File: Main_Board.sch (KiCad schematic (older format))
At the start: 62 parts, among them J1 DAC_12-bits, J2 Measurement_Header, Q1 Q_PNP_BCE, Q2 Q_NPN_BCE, U1 AD667, U2 LF356, U3 AD558JN

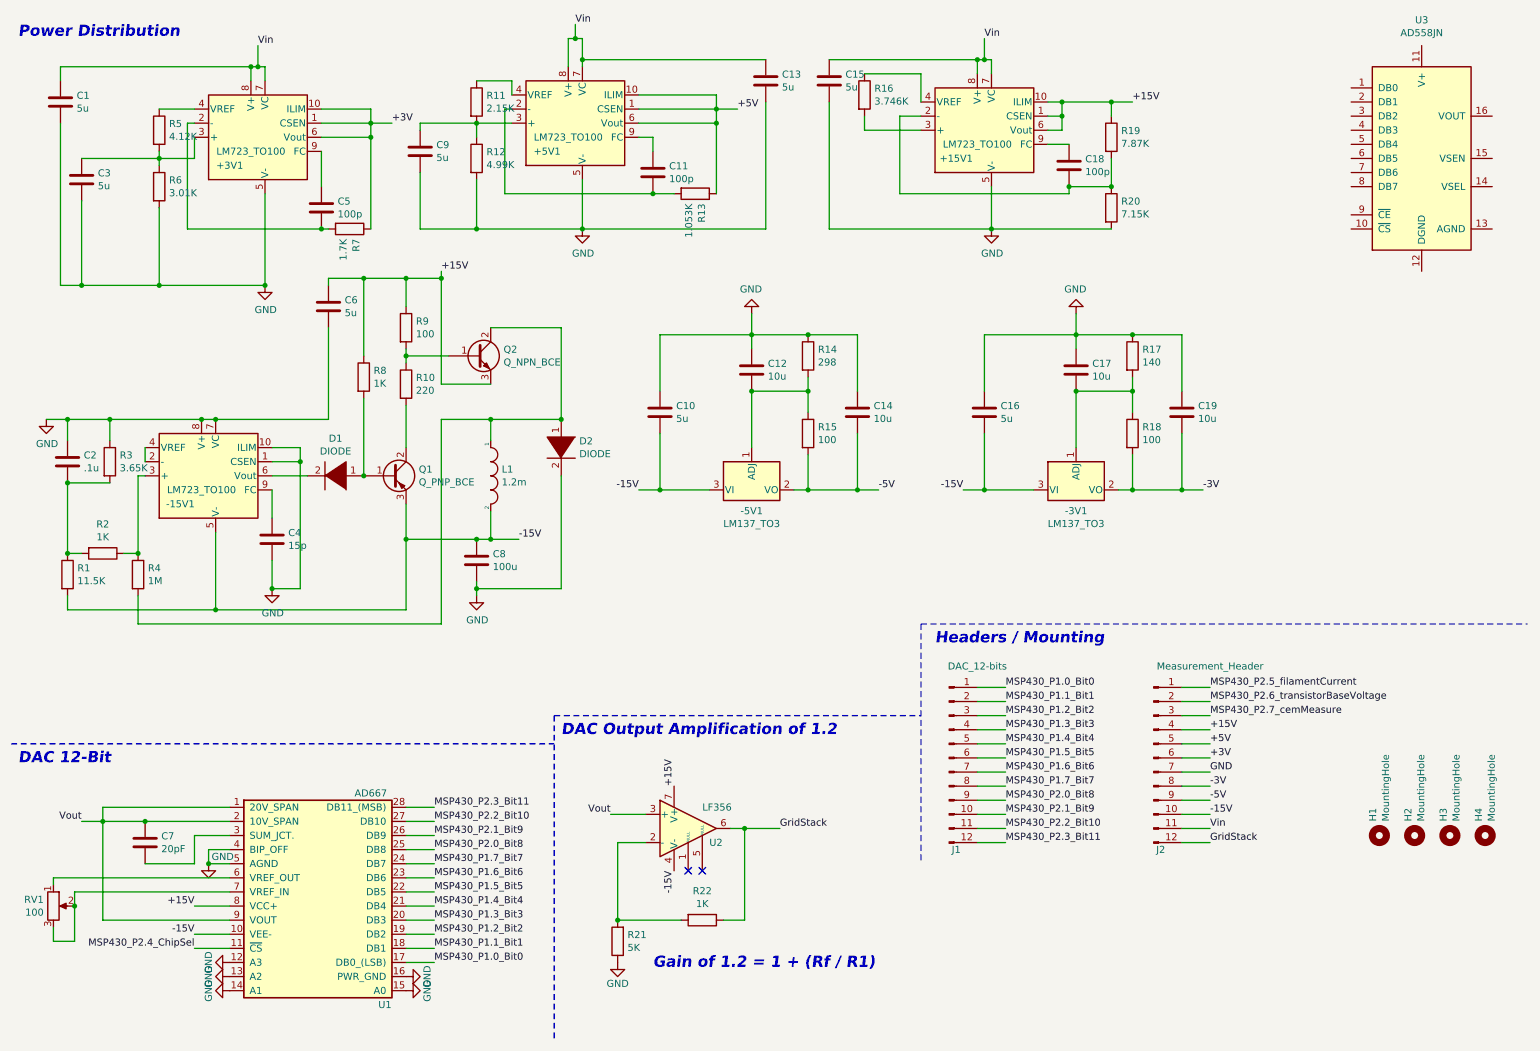
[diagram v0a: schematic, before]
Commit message: Defined and added 8-bit DAC for CEM transistor base voltage control to schematic and  layout. Still need to do the routing, waiting on clarification of analog output voltage range of 0-2.56V or 0-10V from Riya as this will effect 8-bit DAC pin wiring.
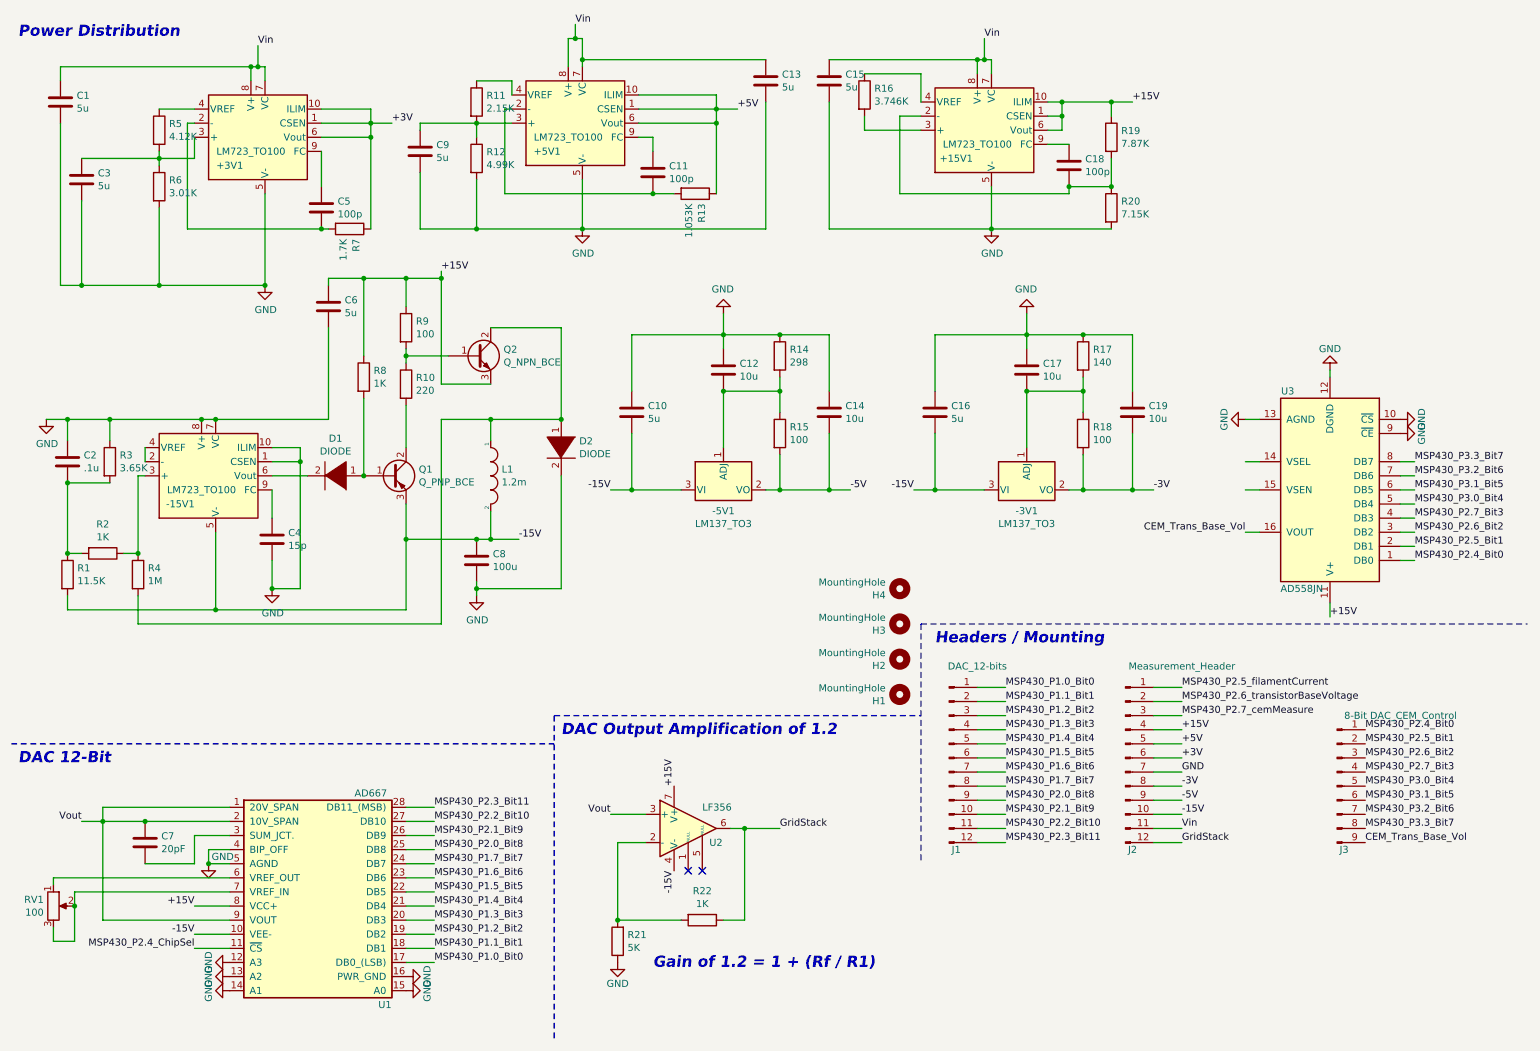
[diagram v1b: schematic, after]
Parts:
- added J3: 8-Bit DAC_CEM_Control, Connector_PinHeader_2.54mm:PinHeader_1x09_P2.54mm_Vertical, symbol Connector:Conn_01x09_Male
- RV1: footprint Potentiometer_THT:Potentiometer_Vishay_148-149_Single_Horizontal -> Potentiometer_THT:Potentiometer_Bourns_3299W_Vertical
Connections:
- net +15V: now also U3.11 (V+)
- net GND: now also U3.10 (~CS), U3.12 (DGND), U3.13 (AGND), U3.9 (~CE)
- net MSP430_P2.4_Bit0: now reaches U3.1 (DB0)
- net MSP430_P2.4_Bit0: now also J3.1 (Pin_1)
- net CEM_Trans_Base_Vol: now reaches U3.16 (VOUT)
- net CEM_Trans_Base_Vol: now also J3.9 (Pin_9)
- net MSP430_P2.5_Bit1: now reaches U3.2 (DB1)
- net MSP430_P2.5_Bit1: now also J3.2 (Pin_2)
- net MSP430_P2.6_Bit2: now reaches U3.3 (DB2)
- net MSP430_P2.6_Bit2: now also J3.3 (Pin_3)
- net MSP430_P2.7_Bit3: now reaches U3.4 (DB3)
- net MSP430_P2.7_Bit3: now also J3.4 (Pin_4)
- net MSP430_P3.0_Bit4: now reaches U3.5 (DB4)
- net MSP430_P3.0_Bit4: now also J3.5 (Pin_5)
- net MSP430_P3.1_Bit5: now reaches U3.6 (DB5)
- net MSP430_P3.1_Bit5: now also J3.6 (Pin_6)
- net MSP430_P3.2_Bit6: now reaches U3.7 (DB6)
- net MSP430_P3.2_Bit6: now also J3.7 (Pin_7)
- net MSP430_P3.3_Bit7: now reaches U3.8 (DB7)
- net MSP430_P3.3_Bit7: now also J3.8 (Pin_8)
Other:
- moved on the sheet: -3V1, -5V1, C10, C12, C14, C16, C17, C19, H1, H2, H3, H4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

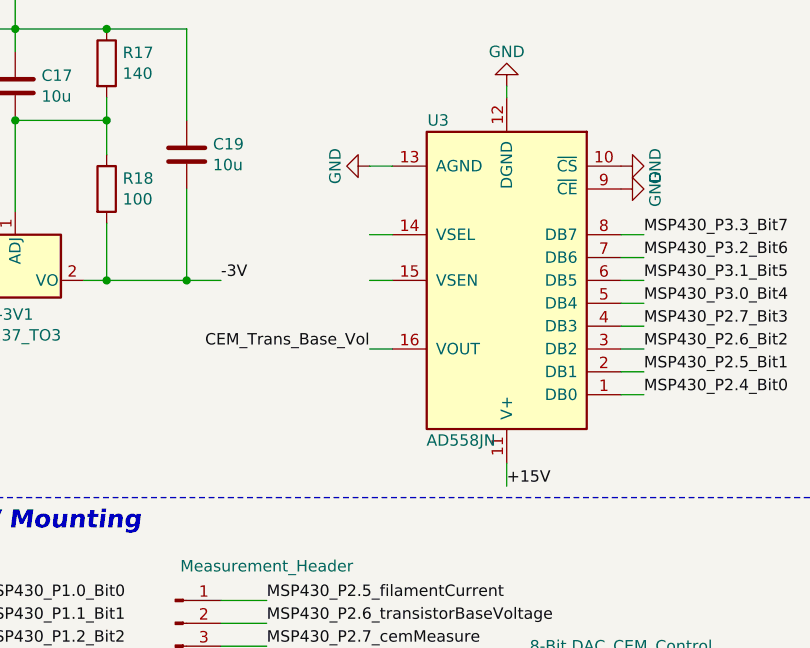
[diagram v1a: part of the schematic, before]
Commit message: Finished schematic and layout of 8-bit DAC for CEM transistor control. Adding GND plane to bottom copper.
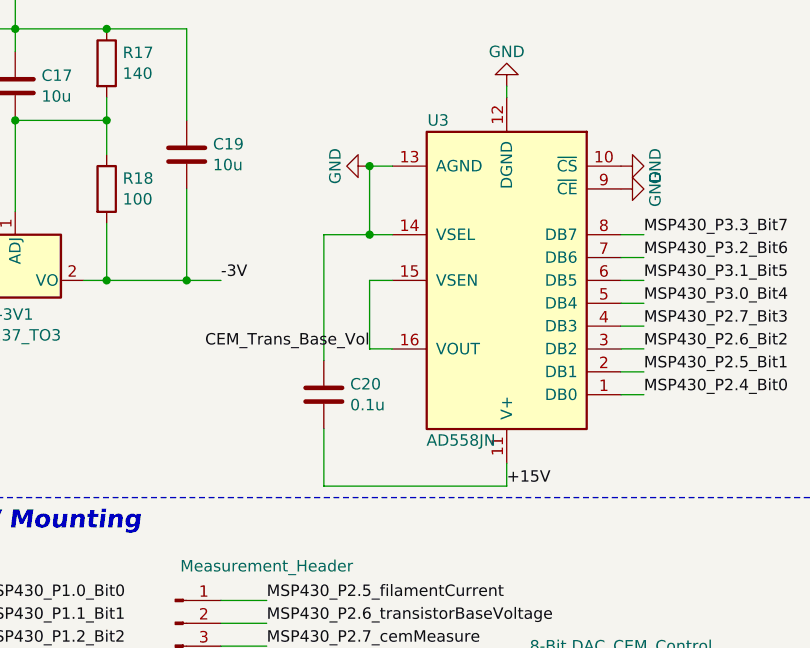
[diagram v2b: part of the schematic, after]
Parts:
- added C20: 0.1u, Capacitor_SMD:C_0805_2012Metric, symbol Device:C
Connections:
- net +15V: now also C20.2
- net CEM_Trans_Base_Vol: now also U3.15 (VSEN)
- net GND: now also U3.14 (VSEL), C20.1
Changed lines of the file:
@@
 Text Label 10100 6400 0    50   ~ 0
 CEM_Trans_Base_Vol
+Wire Wire Line
+	9250 3900 9250 4200
+Wire Wire Line
+	9250 3700 9250 3400
+Connection ~ 9250 3400
+Wire Wire Line
+	9250 3700 9050 3700
+Wire Wire Line
+	9050 4800 9850 4800
+Connection ~ 9250 3700
+$Comp
+L Device:C C20
+U 1 1 5E5EB6F5
+P 9050 4400
+F 0 "C20" H 9165 4446 50  0000 L CNN
+F 1 "0.1u" H 9165 4355 50  0000 L CNN
+F 2 "Capacitor_SMD:C_0805_2012Metric" H 9088 4250 50  0001 C CNN
+F 3 "~" H 9050 4400 50  0001 C CNN
+	1    9050 4400
+	1    0    0    -1
+$EndComp
+Wire Wire Line
+	9050 3700 9050 4250
+Wire Wire Line
+	9050 4800 9050 4550
 $EndSCHEMATC

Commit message: Update Schematic
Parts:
- removed J3: 8-Bit DAC_CEM_Control, Connector_PinHeader_2.54mm:PinHeader_1x09_P2.54mm_Vertical, symbol Connector:Conn_01x09_Male
- added J3: Measurement_Header, Connector_PinHeader_2.54mm:PinHeader_1x12_P2.54mm_Vertical, symbol Connector:Conn_01x12_Male
- J2: value Measurement_Header -> Bias_Header
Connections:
- net CEM_Trans_Base_Vol is gone; now on net MSP430_P2.6_transistorBaseVoltage: U3.15 (VSEN), U3.16 (VOUT)
- net +15V: now also J2.10 (Pin_10); no longer J2.4 (Pin_4)
- net +3V: now also J2.8 (Pin_8); no longer J2.6 (Pin_6)
- net +5V: now also J2.9 (Pin_9); no longer J2.5 (Pin_5)
- net -15V: now also J2.4 (Pin_4); no longer J2.10 (Pin_10)
- net -3V: now also J2.6 (Pin_6); no longer J2.8 (Pin_8)
- net -5V: now also J2.5 (Pin_5); no longer J2.9 (Pin_9)
- net MSP430_P2.4_Bit0: now also J3.1 (Pin_1)
- net MSP430_P2.5_Bit1: now also J3.2 (Pin_2)
- net MSP430_P2.5_filamentCurrent: now also J3.10 (Pin_10); no longer J2.1 (Pin_1)
- net MSP430_P2.6_Bit2: now also J3.3 (Pin_3)
- net MSP430_P2.6_transistorBaseVoltage: now also J3.12 (Pin_12); no longer J2.2 (Pin_2)
- net MSP430_P2.7_Bit3: now also J3.4 (Pin_4)
- net MSP430_P2.7_cemMeasure: now also J3.11 (Pin_11); no longer J2.3 (Pin_3)
- net MSP430_P3.0_Bit4: now also J3.5 (Pin_5)
- net MSP430_P3.1_Bit5: now also J3.6 (Pin_6)
- net MSP430_P3.2_Bit6: now also J3.7 (Pin_7)
- net MSP430_P3.3_Bit7: now also J3.8 (Pin_8)
- new net -200V: J2.1 (Pin_1)
- no-connect marks 2 -> 5
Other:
- moved on the sheet: H1, H2, H3, H4
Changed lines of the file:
@@
 EESchema Schematic File Version 4
+LIBS:Main_Board-cache
 EELAYER 30 0
 EELAYER END
@@
 P 8400 5800
 F 0 "J2" H 8450 5150 50  0000 C CNN
-F 1 "Measurement_Header" H 8800 6450 50  0000 C CNN
+F 1 "Bias_Header" H 8800 6450 50  0000 C CNN
 F 2 "Connector_PinHeader_2.54mm:PinHeader_1x12_P2.54mm_Vertical" H 8400 5800 50  0001 C CNN
 F 3 "~" H 8400 5800 50  0001 C CNN
@@
 L Mechanical:MountingHole H1
 U 1 1 5E4EA3AF
-P 6800 5350
-F 0 "H1" H 6900 5396 50  0000 L CNN
-F 1 "MountingHole" H 6900 5305 50  0000 L CNN
-F 2 "MountingHole:MountingHole_3.5mm" H 6800 5350 50  0001 C CNN
-F 3 "~" H 6800 5350 50  0001 C CNN
-	1    6800 5350
+P 11050 5800
+F 0 "H1" H 11150 5846 50  0000 L CNN
+F 1 "MountingHole" H 11150 5755 50  0000 L CNN
+F 2 "MountingHole:MountingHole_3.5mm" H 11050 5800 50  0001 C CNN
+F 3 "~" H 11050 5800 50  0001 C CNN
+	1    11050 5800
 	-1   0    0    1
 $EndComp
@@
 L Mechanical:MountingHole H2
 U 1 1 5E4EB209
-P 6800 5100
-F 0 "H2" H 6900 5146 50  0000 L CNN
-F 1 "MountingHole" H 6900 5055 50  0000 L CNN
-F 2 "MountingHole:MountingHole_3.5mm" H 6800 5100 50  0001 C CNN
-F 3 "~" H 6800 5100 50  0001 C CNN
-	1    6800 5100
+P 11050 5550
+F 0 "H2" H 11150 5596 50  0000 L CNN
+F 1 "MountingHole" H 11150 5505 50  0000 L CNN
+F 2 "MountingHole:MountingHole_3.5mm" H 11050 5550 50  0001 C CNN
+F 3 "~" H 11050 5550 50  0001 C CNN
+	1    11050 5550
 	-1   0    0    1
 $EndComp
@@
 L Mechanical:MountingHole H3
 U 1 1 5E4EB42E
-P 6800 4850
-F 0 "H3" H 6900 4896 50  0000 L CNN
-F 1 "MountingHole" H 6900 4805 50  0000 L CNN
-F 2 "MountingHole:MountingHole_3.5mm" H 6800 4850 50  0001 C CNN
-F 3 "~" H 6800 4850 50  0001 C CNN
-	1    6800 4850
+P 11050 5300
+F 0 "H3" H 11150 5346 50  0000 L CNN
+F 1 "MountingHole" H 11150 5255 50  0000 L CNN
+F 2 "MountingHole:MountingHole_3.5mm" H 11050 5300 50  0001 C CNN
+F 3 "~" H 11050 5300 50  0001 C CNN
+	1    11050 5300
 	-1   0    0    1
 $EndComp
@@
 L Mechanical:MountingHole H4
 U 1 1 5E4EB541
-P 6800 4600
-F 0 "H4" H 6900 4646 50  0000 L CNN
-F 1 "MountingHole" H 6900 4555 50  0000 L CNN
-F 2 "MountingHole:MountingHole_3.5mm" H 6800 4600 50  0001 C CNN
-F 3 "~" H 6800 4600 50  0001 C CNN
-	1    6800 4600
+P 11050 5050
+F 0 "H4" H 11150 5096 50  0000 L CNN
+F 1 "MountingHole" H 11150 5005 50  0000 L CNN
+F 2 "MountingHole:MountingHole_3.5mm" H 11050 5050 50  0001 C CNN
+F 3 "~" H 11050 5050 50  0001 C CNN
+	1    11050 5050
 	-1   0    0    1
 $EndComp
@@
 Wire Wire Line
 	8600 6400 8800 6400
-Text Label 8800 5300 0    50   ~ 0
-MSP430_P2.5_filamentCurrent
-Text Label 8800 5400 0    50   ~ 0
-MSP430_P2.6_transistorBaseVoltage
-Text Label 8800 5500 0    50   ~ 0
-MSP430_P2.7_cemMeasure
 Text Notes 7050 5000 0    79   Italic 16
 Headers / Mounting
@@
 Gain of 1.2 = 1 + (Rf / R1)
 Text Label 8800 5600 0    50   ~ 0
-+15V
+-15V
 Text Label 8800 5700 0    50   ~ 0
-+5V
+-5V
 Text Label 8800 5800 0    50   ~ 0
-+3V
+-3V
 Text Label 8800 5900 0    50   ~ 0
 GND
 Text Label 8800 6000 0    50   ~ 0
--3V
++3V
 Text Label 8800 6100 0    50   ~ 0
--5V
++5V
 Text Label 8800 6200 0    50   ~ 0
--15V
++15V
 Text Label 8800 6300 0    50   ~ 0
 Vin
@@
 	8000 1800 8000 1750
 Connection ~ 8000 1750
-Text Label 9250 4200 2    50   ~ 0
-CEM_Trans_Base_Vol
 Text Label 10450 3700 0    50   ~ 0
 MSP430_P3.3_Bit7
@@
 Text Label 9850 4800 0    50   ~ 0
 +15V
-$Comp
-L Connector:Conn_01x09_Male J3
-U 1 1 5E7C84B4
-P 9900 6000
-F 0 "J3" H 9950 5550 50  0000 C CNN
-F 1 "8-Bit DAC_CEM_Control" H 10350 6500 50  0000 C CNN
-F 2 "Connector_PinHeader_2.54mm:PinHeader_1x09_P2.54mm_Vertical" H 9900 6000 50  0001 C CNN
-F 3 "~" H 9900 6000 50  0001 C CNN
-	1    9900 6000
-	1    0    0    -1
-$EndComp
-Text Label 10100 5600 0    50   ~ 0
+Text Label 9600 5300 0    50   ~ 0
 MSP430_P2.4_Bit0
-Text Label 10100 5700 0    50   ~ 0
+Text Label 9600 5400 0    50   ~ 0
 MSP430_P2.5_Bit1
-Text Label 10100 5800 0    50   ~ 0
+Text Label 9600 5500 0    50   ~ 0
 MSP430_P2.6_Bit2
-Text Label 10100 5900 0    50   ~ 0
+Text Label 9600 5600 0    50   ~ 0
 MSP430_P2.7_Bit3
-Text Label 10100 6000 0    50   ~ 0
+Text Label 9600 5700 0    50   ~ 0
 MSP430_P3.0_Bit4
-Text Label 10100 6100 0    50   ~ 0
+Text Label 9600 5800 0    50   ~ 0
 MSP430_P3.1_Bit5
-Text Label 10100 6200 0    50   ~ 0
+Text Label 9600 5900 0    50   ~ 0
 MSP430_P3.2_Bit6
-Text Label 10100 6300 0    50   ~ 0
+Text Label 9600 6000 0    50   ~ 0
 MSP430_P3.3_Bit7
-Text Label 10100 6400 0    50   ~ 0
-CEM_Trans_Base_Vol
-Wire Wire Line
-	9250 3900 9250 4200
 Wire Wire Line
 	9250 3700 9250 3400
@@
 Wire Wire Line
 	9050 4800 9050 4550
+Text Label 9600 6400 0    50   ~ 0
+MSP430_P2.6_transistorBaseVoltage
+Text Label 8100 4100 0    50   ~ 0
+MSP430_P2.6_transistorBaseVoltage
+Wire Wire Line
+	8100 4100 9250 4100
+Wire Wire Line
+	9250 3900 9250 4100
+Connection ~ 9250 4100
+Wire Wire Line
+	9250 4100 9250 4200
+$Comp
+L Connector:Conn_01x12_Male J3
+U 1 1 5E603C7A
+P 9400 5800
+F 0 "J3" H 9450 5150 50  0000 C CNN
+F 1 "Measurement_Header" H 9800 6450 50  0000 C CNN
+F 2 "Connector_PinHeader_2.54mm:PinHeader_1x12_P2.54mm_Vertical" H 9400 5800 50  0001 C CNN
+F 3 "~" H 9400 5800 50  0001 C CNN
+	1    9400 5800
+	1    0    0    -1
+$EndComp
+Text Label 9600 6200 0    50   ~ 0
+MSP430_P2.5_filamentCurrent
+Text Label 9600 6300 0    50   ~ 0
+MSP430_P2.7_cemMeasure
+NoConn ~ 8800 5500
+NoConn ~ 8800 5400
+NoConn ~ 9600 6100
+Text Label 8800 5300 0    50   ~ 0
+-200V
 $EndSCHEMATC

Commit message: Pins
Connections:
- net +15V: now also J2.3 (Pin_3); no longer J2.10 (Pin_10)
- net +3V: now also J2.5 (Pin_5); no longer J2.8 (Pin_8)
- net +5V: now also J2.4 (Pin_4); no longer J2.9 (Pin_9)
- net -15V: now also J2.9 (Pin_9); no longer J2.4 (Pin_4)
- net -200V: now also J2.12 (Pin_12); no longer J2.1 (Pin_1)
- net -3V: now also J2.7 (Pin_7); no longer J2.6 (Pin_6)
- net -5V: now also J2.8 (Pin_8); no longer J2.5 (Pin_5)
- net GND: now also J2.6 (Pin_6); no longer J2.7 (Pin_7)
- net GridStack: now also J2.1 (Pin_1); no longer J2.12 (Pin_12)
- net Vin: now also J2.2 (Pin_2); no longer J2.11 (Pin_11)
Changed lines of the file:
@@
 Text Notes 5050 7300 0    79   Italic 16
 Gain of 1.2 = 1 + (Rf / R1)
+Text Label 8800 6100 0    50   ~ 0
+-15V
+Text Label 8800 6000 0    50   ~ 0
+-5V
+Text Label 8800 5900 0    50   ~ 0
+-3V
+Text Label 8800 5800 0    50   ~ 0
+GND
+Text Label 8800 5700 0    50   ~ 0
++3V
 Text Label 8800 5600 0    50   ~ 0
--15V
-Text Label 8800 5700 0    50   ~ 0
--5V
-Text Label 8800 5800 0    50   ~ 0
--3V
-Text Label 8800 5900 0    50   ~ 0
-GND
-Text Label 8800 6000 0    50   ~ 0
-+3V
-Text Label 8800 6100 0    50   ~ 0
 +5V
-Text Label 8800 6200 0    50   ~ 0
+Text Label 8800 5500 0    50   ~ 0
 +15V
-Text Label 8800 6300 0    50   ~ 0
+Text Label 8800 5400 0    50   ~ 0
 Vin
-Text Label 8800 6400 0    50   ~ 0
+Text Label 8800 5300 0    50   ~ 0
 GridStack
 Text Notes 4400 5650 0    79   Italic 16
@@
 Text Label 9600 6300 0    50   ~ 0
 MSP430_P2.7_cemMeasure
-NoConn ~ 8800 5500
-NoConn ~ 8800 5400
 NoConn ~ 9600 6100
-Text Label 8800 5300 0    50   ~ 0
+Text Label 8800 6400 0    50   ~ 0
 -200V
+NoConn ~ 8800 6200
+NoConn ~ 8800 6300
 $EndSCHEMATC
